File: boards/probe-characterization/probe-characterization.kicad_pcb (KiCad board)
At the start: 2 copper layers, 25 x 74.9 mm, 17 parts, among them J1 SMA, J10 PROBE, J11 PROBE, J2 SMA, J3 SMA, J4 SMA, J5 SMA, J6 SMA, J7 SMA, J8 SMA, J9 SMA

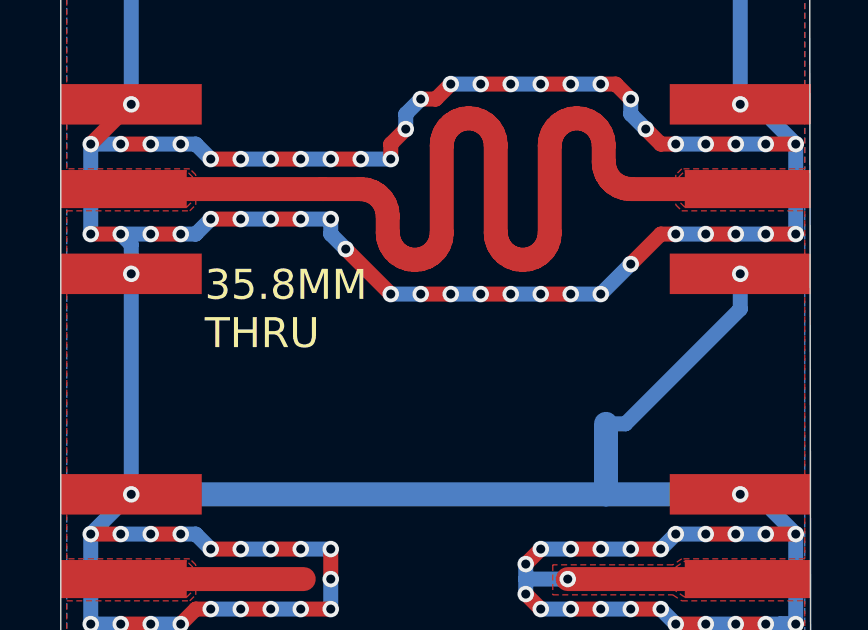
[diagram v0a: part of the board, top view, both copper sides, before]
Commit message: Finished probe-characterization board
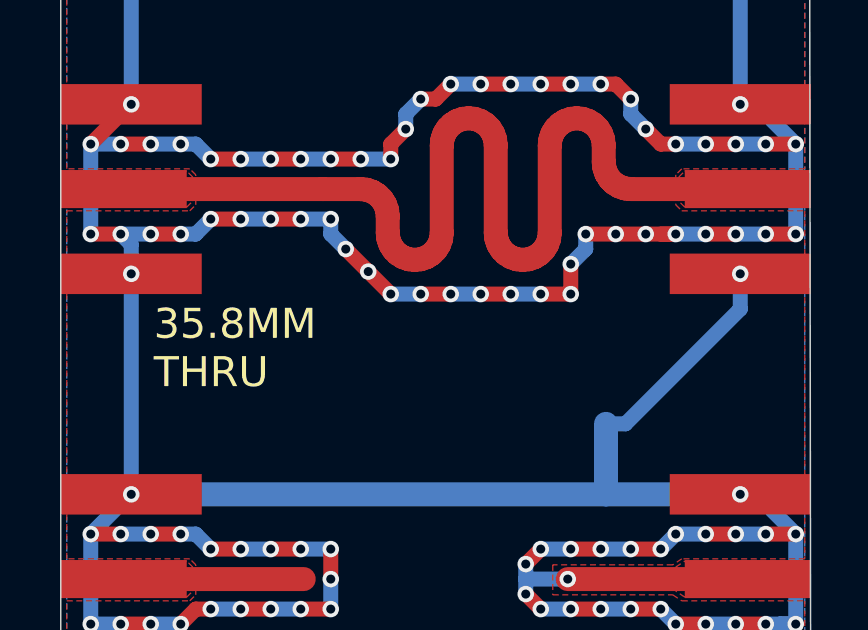
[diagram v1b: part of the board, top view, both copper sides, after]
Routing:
- net /GND: track 660.0 -> 661.4 mm, vias 347 -> 350
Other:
- board text added: "Place UL mark and date code in this area"

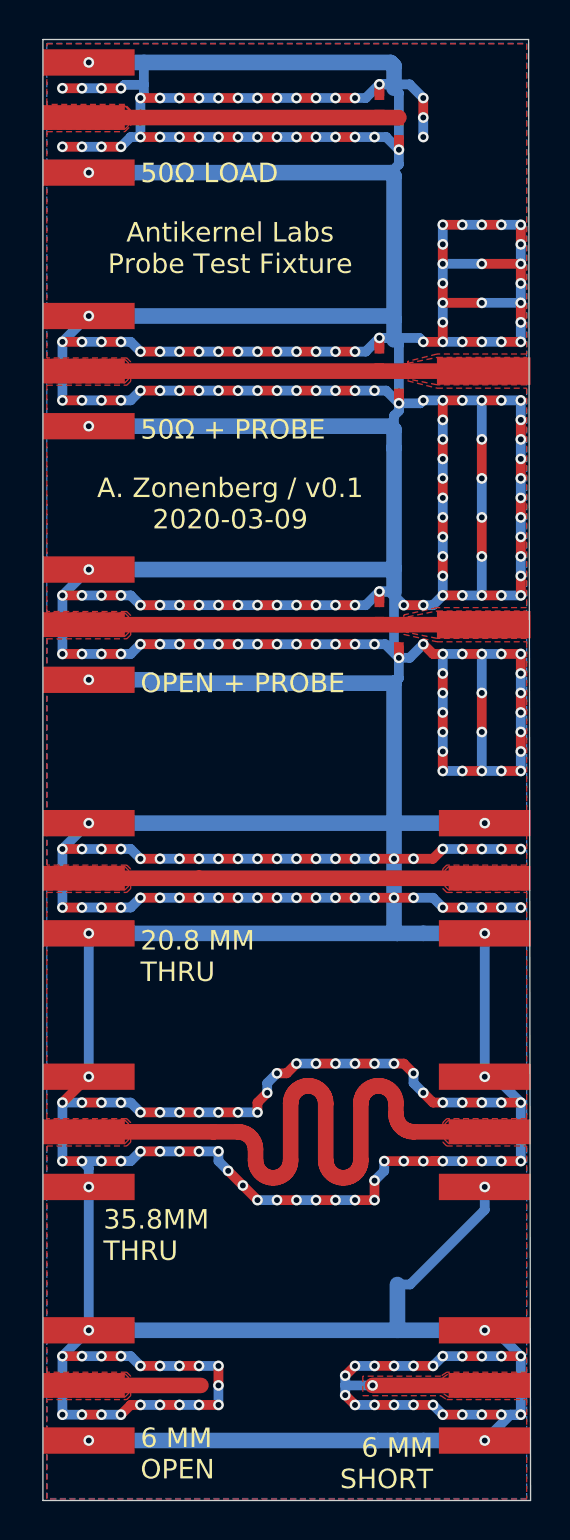
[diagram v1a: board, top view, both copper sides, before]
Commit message: Updated probe-characterization with some fab DRC fixes (ground too close to ground SMA pad, right edge not quite vertical)
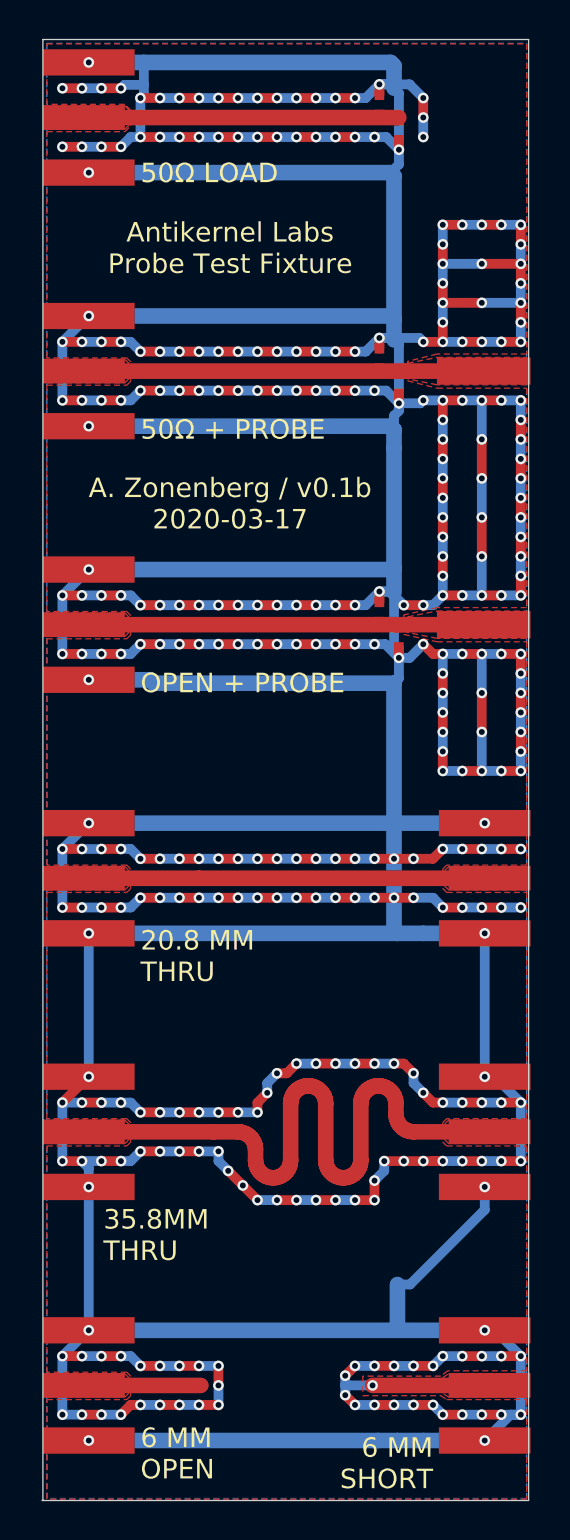
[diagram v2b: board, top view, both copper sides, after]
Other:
- board size 25 x 74.9 mm -> 24.9 x 74.9 mm
- board text added: "A. Zonenberg / v0.1b 2020-03-17"
- board text removed: "A. Zonenberg / v0.1 2020-03-09"
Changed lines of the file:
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@@
   )
   (setup
-    (last_trace_width 0.5)
+    (last_trace_width 0.8)
     (user_trace_width 0.5)
     (user_trace_width 0.8)
@@
     (effects (font (size 1 1) (thickness 0.1)) (justify left))
   )
-  (gr_text "A. Zonenberg / v0.1\n2020-03-09" (at 39.6 59.8) (layer F.SilkS)
+  (gr_text "A. Zonenberg / v0.1b\n2020-03-17" (at 39.6 59.8) (layer F.SilkS)
     (effects (font (size 1 1) (thickness 0.1)))
   )
@@
   )
   (gr_line (start 54.9 36) (end 30 36) (layer Edge.Cuts) (width 0.05))
-  (gr_line (start 55 110.9) (end 54.9 36) (layer Edge.Cuts) (width 0.05))
-  (gr_line (start 30 110.9) (end 55 110.9) (layer Edge.Cuts) (width 0.05))
+  (gr_line (start 54.9 110.9) (end 54.9 36) (layer Edge.Cuts) (width 0.05))
+  (gr_line (start 29.95 110.9) (end 54.9 110.9) (layer Edge.Cuts) (width 0.05))
   (gr_line (start 30 36) (end 30 110.9) (layer Edge.Cuts) (width 0.05))
-  (segment (start 32.1 105) (end 38.1 105) (width 0.8) (layer F.Cu) (net 7))
   (via (at 32.35 37.175) (size 0.55) (drill 0.3) (layers F.Cu B.Cu) (net 1))
   (via (at 32.35 42.825) (size 0.55) (drill 0.3) (layers F.Cu B.Cu) (net 1))
@@
   (segment (start 45.600268 94.339) (end 45.4 94.361564) (width 0.8) (layer F.Cu) (net 6))
   (segment (start 45.4 94.361564) (end 45.199731 94.339) (width 0.8) (layer F.Cu) (net 6))
+  (segment (start 32.1 105) (end 38.1 105) (width 0.8) (layer F.Cu) (net 7))
   (zone (net 1) (net_name /GND) (layer B.Cu) (hatch edge 0.508)
     (connect_pads (clearance 0.1))
@@
         (xy 50.5 78.525) (xy 50.5 79.525) (xy 50.7 79.725) (xy 54.8 79.725) (xy 54.8 91.325)
         (xy 50.7 91.325) (xy 50.5 91.525) (xy 50.5 92.525) (xy 50.7 92.725) (xy 54.8 92.725)
-        (xy 54.8 104.325) (xy 50.7 104.325) (xy 50.4 104.525) (xy 46.4 104.525) (xy 46.4 105.525)
+        (xy 54.8 104.25) (xy 50.75 104.25) (xy 50.4 104.525) (xy 46.4 104.525) (xy 46.4 105.525)
         (xy 50.4 105.525) (xy 50.7 105.725) (xy 54.8 105.725) (xy 54.8 110.825) (xy 30.2 110.825)
         (xy 30.2 105.725) (xy 34.3 105.725) (xy 34.5 105.525) (xy 34.5 104.525) (xy 34.3 104.325)
